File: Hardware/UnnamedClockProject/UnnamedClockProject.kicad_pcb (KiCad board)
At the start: 2 copper layers, 160 x 102 mm, 38 parts, among them J101 CLOCK_OUT, J102 POWER, J103 BUTTONS, Q101 2N3904, U104 G3MB-202P, U105 G3MB-202P, U106 G3MB-202P, U107 CAT24C256

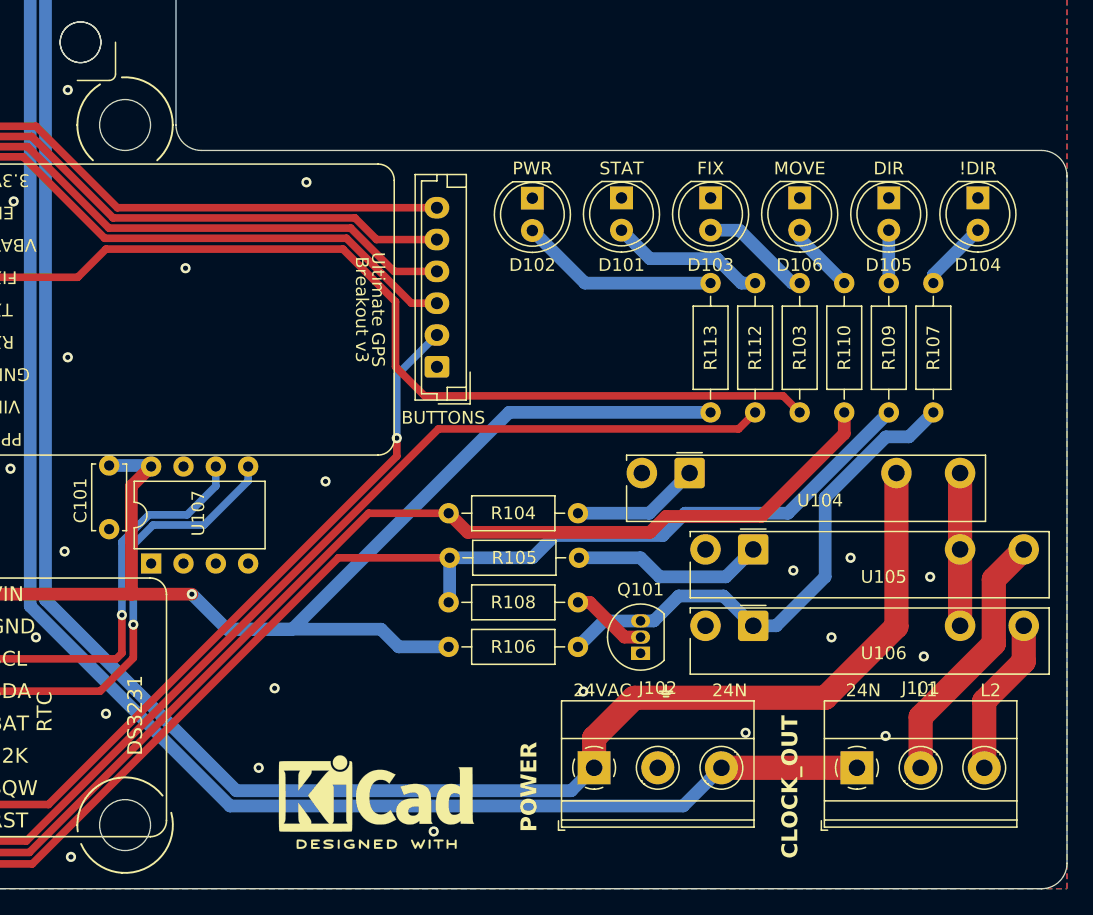
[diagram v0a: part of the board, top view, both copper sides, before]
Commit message: Fix optorelays not fitting (#8)
This is fine for now, merging mostly because so many code improvements now depend on this branch!
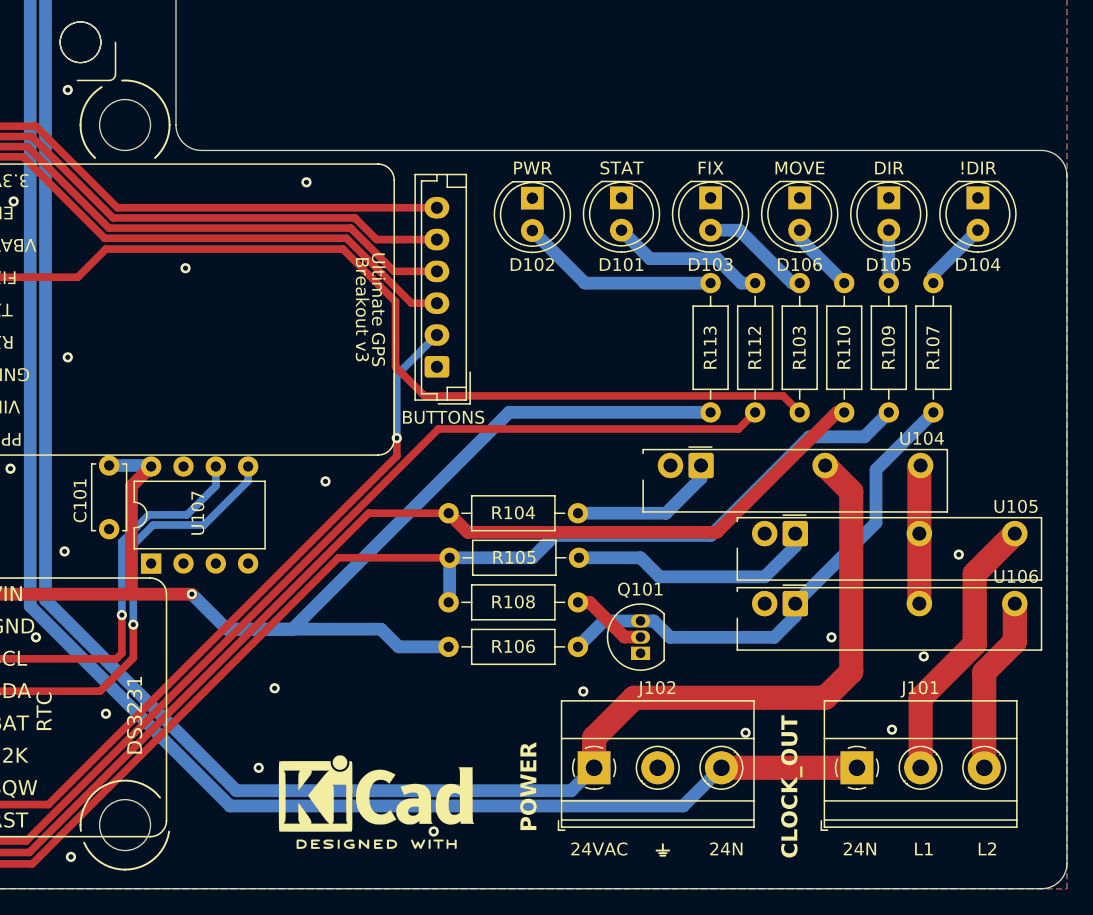
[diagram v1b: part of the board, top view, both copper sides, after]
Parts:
- U104, U105, U106: footprint OptoDevice:Finder_34.81 -> ac1ja:OptoRelay
- moved U106 10.7 mm to (54.0, 38.8)
- moved U105 10.7 mm to (54.0, 33.2)
- moved U104 8.27 mm to (46.6, 27.9)
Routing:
- net Net-(R105-Pad2): track 15.2 -> 19.6 mm
- net Net-(R104-Pad2): track 10.1 -> 11.8 mm
- net /NOT_DIR: track 41.1 -> 39.6 mm
- net /L2_OUT: track 11.9 -> 13.4 mm
- net Net-(U104-Pad14): track 12.0 -> 10.9 mm
- net /EN: track 145.5 -> 144.5 mm
- net /L1_OUT: track 20.0 -> 21.0 mm
- net GND: vias 60 -> 58
